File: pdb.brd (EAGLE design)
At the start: 50 x 85 mm, 38 parts, among them Q1 20MHz, Q2 IRFR5305PBF, Q3 IRFR5305PBF, U1 TSR_1-2433, U2 LTC2946CMSPBF, U3 LTC2946CMSPBF, U4 LTC2946CMSPBF, U5 ATMEGA48-20AU, U6 TXB0104, U7 AT30TS74SS8M

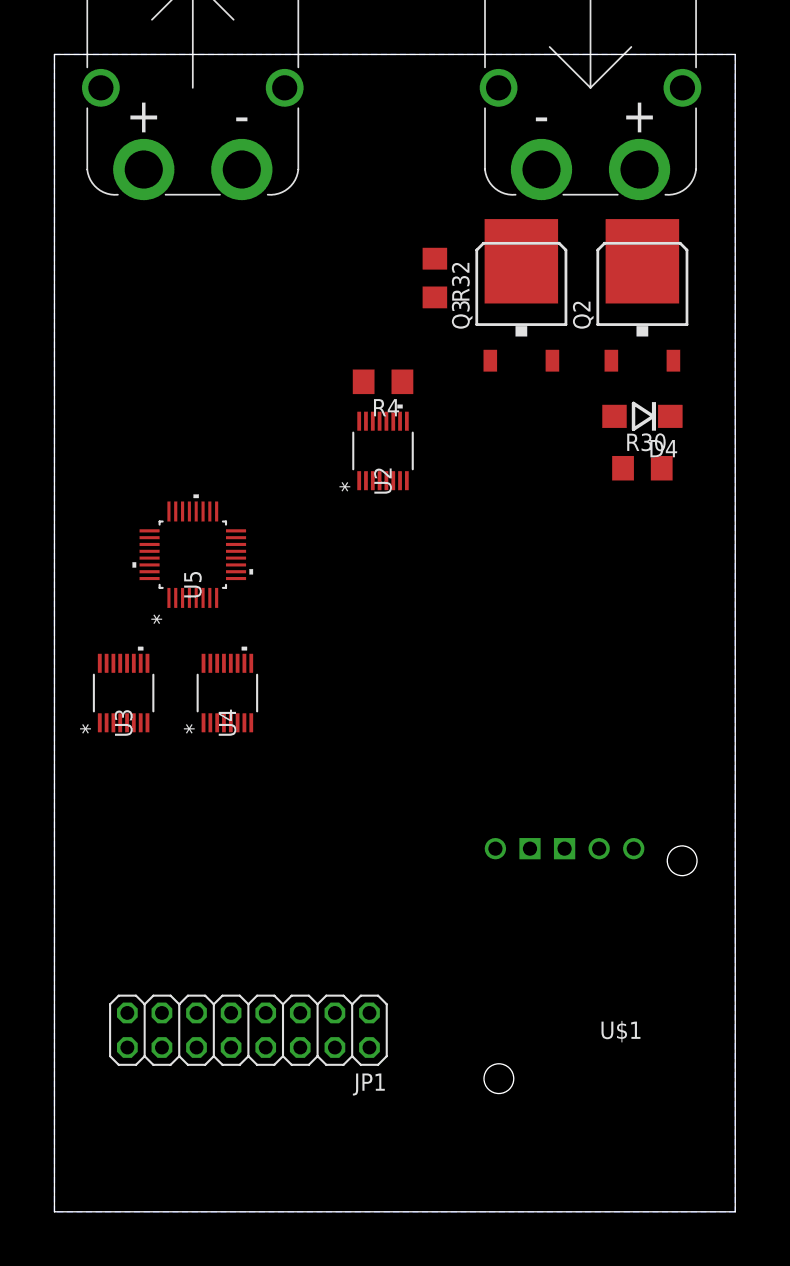
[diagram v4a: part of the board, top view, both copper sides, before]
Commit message: added mounting holes
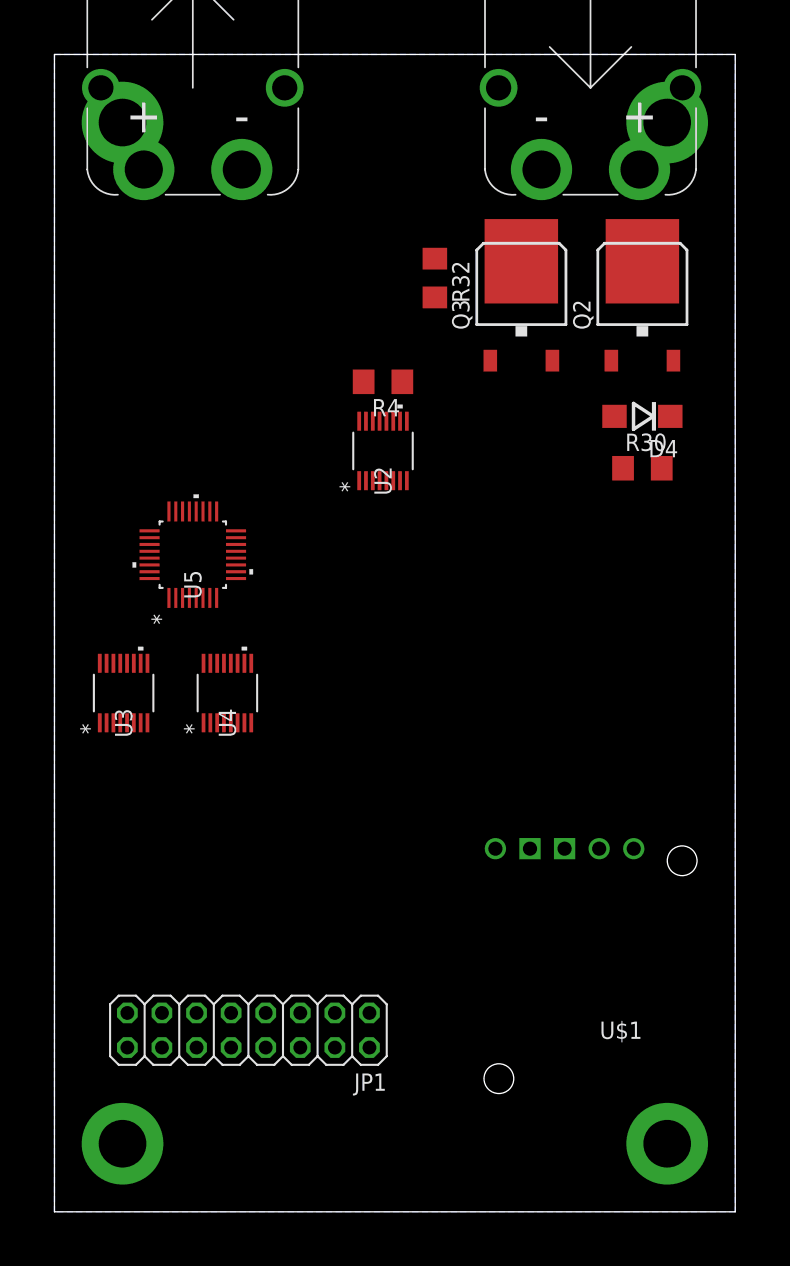
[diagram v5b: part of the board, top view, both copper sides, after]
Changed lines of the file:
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@@
 <element name="L1" library="rcl" package="0204/7" value="100µH" x="97.79" y="-7.62" rot="R90"/>
 <element name="ESC" library="amass" package="XT60PWFEMALE" value="XT60PWFEMALE" x="10.16" y="82.55"/>
-<element name="JP1" library="pinhead" library_urn="urn:adsk.eagle:library:325" package="2X08" package3d_urn="urn:adsk.eagle:package:22481/2" value="" x="14.245" y="13.335" rot="R180"/>
+<element name="JP1" library="pinhead" library_urn="urn:adsk.eagle:library:325" package="2X08" package3d_urn="urn:adsk.eagle:package:22481/2" value="" x="14.245" y="13.335" locked="yes" rot="R180"/>
 <element name="U7" library="jonas_microchip" library_urn="urn:adsk.eagle:library:891228" package="SO08" package3d_urn="urn:adsk.eagle:package:1422804/3" value="AT30TS74SS8M" x="-21.59" y="-24.13"/>
 <element name="L2" library="jonas_bourns" library_urn="urn:adsk.eagle:library:1422904" package="IND_BOURNS_RLB9012" package3d_urn="urn:adsk.eagle:package:1422907/3" value="RLB9012-221KL" x="-12.7" y="-38.1">
@@
 <vertex x="0" y="0"/>
 </polygon>
-<wire x1="37.465" y1="26.67" x2="34.925" y2="26.67" width="0" layer="19" extent="1-1"/>
-<wire x1="77.47" y1="20.32" x2="37.465" y2="26.67" width="0" layer="19" extent="1-1"/>
-<wire x1="81.96" y1="4.7022" x2="77.47" y2="20.32" width="0" layer="19" extent="1-1"/>
+<via x="5" y="80" extent="1-16" drill="3.5" diameter="6" locked="yes"/>
+<via x="45" y="80" extent="1-16" drill="3.5" diameter="6" locked="yes"/>
+<via x="5" y="5" extent="1-16" drill="3.5" diameter="6" locked="yes"/>
+<via x="45" y="5" extent="1-16" drill="3.5" diameter="6" locked="yes"/>
+<wire x1="35.77" y1="76.55" x2="27.94" y2="70.002" width="0" layer="19" extent="1-1"/>
+<wire x1="3.39" y1="-6.35" x2="5" y2="5" width="0" layer="19" extent="1-1"/>
+<wire x1="3.39" y1="-10.16" x2="3.39" y2="-6.35" width="0" layer="19" extent="1-1"/>
+<wire x1="4.33" y1="-17.78" x2="3.39" y2="-10.16" width="0" layer="19" extent="1-1"/>
+<wire x1="4.33" y1="-22.86" x2="4.33" y2="-17.78" width="0" layer="19" extent="1-1"/>
+<wire x1="4.33" y1="-27.94" x2="4.33" y2="-22.86" width="0" layer="19" extent="1-1"/>
+<wire x1="24.88056875" y1="58.0644" x2="27.94" y2="70.002" width="0" layer="19" extent="1-1"/>
+<wire x1="24.380190625" y1="58.0644" x2="24.88056875" y2="58.0644" width="0" layer="19" extent="1-1"/>
+<wire x1="23.37943125" y1="58.0644" x2="24.380190625" y2="58.0644" width="0" layer="19" extent="1-1"/>
+<wire x1="9.909809375" y1="51.435" x2="23.37943125" y2="58.0644" width="0" layer="19" extent="1-1"/>
+<wire x1="10.410190625" y1="45.085" x2="9.909809375" y2="51.435" width="0" layer="19" extent="1-1"/>
+<wire x1="9.40943125" y1="45.085" x2="10.410190625" y2="45.085" width="0" layer="19" extent="1-1"/>
+<wire x1="13.45056875" y1="40.2844" x2="10.410190625" y2="45.085" width="0" layer="19" extent="1-1"/>
+<wire x1="5.83056875" y1="40.2844" x2="9.40943125" y2="45.085" width="0" layer="19" extent="1-1"/>
+<wire x1="5.330190625" y1="40.2844" x2="5.83056875" y2="40.2844" width="0" layer="19" extent="1-1"/>
+<wire x1="22.01" y1="-17.78" x2="4.33" y2="-17.78" width="0" layer="19" extent="1-1"/>
+<wire x1="45" y1="5" x2="37.465" y2="26.67" width="0" layer="19" extent="1-1"/>
+<wire x1="63.08" y1="0" x2="45" y2="5" width="0" layer="19" extent="1-1"/>
+<wire x1="81.96" y1="4.7022" x2="63.08" y2="0" width="0" layer="19" extent="1-1"/>
+<wire x1="77.47" y1="20.32" x2="81.96" y2="4.7022" width="0" layer="19" extent="1-1"/>
 <wire x1="83.82" y1="-14.39" x2="81.96" y2="4.7022" width="0" layer="19" extent="1-1"/>
 <wire x1="87.63" y1="-14.39" x2="83.82" y2="-14.39" width="0" layer="19" extent="1-1"/>
@@
 <wire x1="73.66" y1="-25.82" x2="77.47" y2="-25.82" width="0" layer="19" extent="1-1"/>
 <wire x1="69.85" y1="-25.82" x2="73.66" y2="-25.82" width="0" layer="19" extent="1-1"/>
-<wire x1="63.08" y1="0" x2="81.96" y2="4.7022" width="0" layer="19" extent="1-1"/>
 <wire x1="107.95" y1="-17.91" x2="87.63" y2="-14.39" width="0" layer="19" extent="1-1"/>
-<wire x1="13.45056875" y1="40.2844" x2="37.465" y2="26.67" width="0" layer="19" extent="1-1"/>
-<wire x1="5.83056875" y1="40.2844" x2="13.45056875" y2="40.2844" width="0" layer="19" extent="1-1"/>
-<wire x1="5.330190625" y1="40.2844" x2="5.83056875" y2="40.2844" width="0" layer="19" extent="1-1"/>
-<wire x1="9.909809375" y1="51.435" x2="5.330190625" y2="40.2844" width="0" layer="19" extent="1-1"/>
-<wire x1="10.410190625" y1="45.085" x2="9.909809375" y2="51.435" width="0" layer="19" extent="1-1"/>
-<wire x1="9.40943125" y1="45.085" x2="10.410190625" y2="45.085" width="0" layer="19" extent="1-1"/>
-<wire x1="24.88056875" y1="58.0644" x2="5.330190625" y2="40.2844" width="0" layer="19" extent="1-1"/>
-<wire x1="24.380190625" y1="58.0644" x2="24.88056875" y2="58.0644" width="0" layer="19" extent="1-1"/>
-<wire x1="23.37943125" y1="58.0644" x2="24.380190625" y2="58.0644" width="0" layer="19" extent="1-1"/>
-<wire x1="27.94" y1="70.002" x2="24.88056875" y2="58.0644" width="0" layer="19" extent="1-1"/>
-<wire x1="35.77" y1="76.55" x2="27.94" y2="70.002" width="0" layer="19" extent="1-1"/>
-<wire x1="3.39" y1="-6.35" x2="9.40943125" y2="45.085" width="0" layer="19" extent="1-1"/>
-<wire x1="3.39" y1="-10.16" x2="3.39" y2="-6.35" width="0" layer="19" extent="1-1"/>
-<wire x1="4.33" y1="-17.78" x2="3.39" y2="-10.16" width="0" layer="19" extent="1-1"/>
-<wire x1="4.33" y1="-22.86" x2="4.33" y2="-17.78" width="0" layer="19" extent="1-1"/>
-<wire x1="4.33" y1="-27.94" x2="4.33" y2="-22.86" width="0" layer="19" extent="1-1"/>
-<wire x1="22.01" y1="-17.78" x2="4.33" y2="-17.78" width="0" layer="19" extent="1-1"/>
 </signal>
 <signal name="V+">
@@
 packages will not be understood (or retained) with this version.
 </note>
+<note version="8.5" severity="warning">
+Since Version 8.5, EAGLE supports locking for holes, vias, wires and polygons.
+The locking property on all objects of these types will not be understood in this version.
+</note>
 </compatibility>

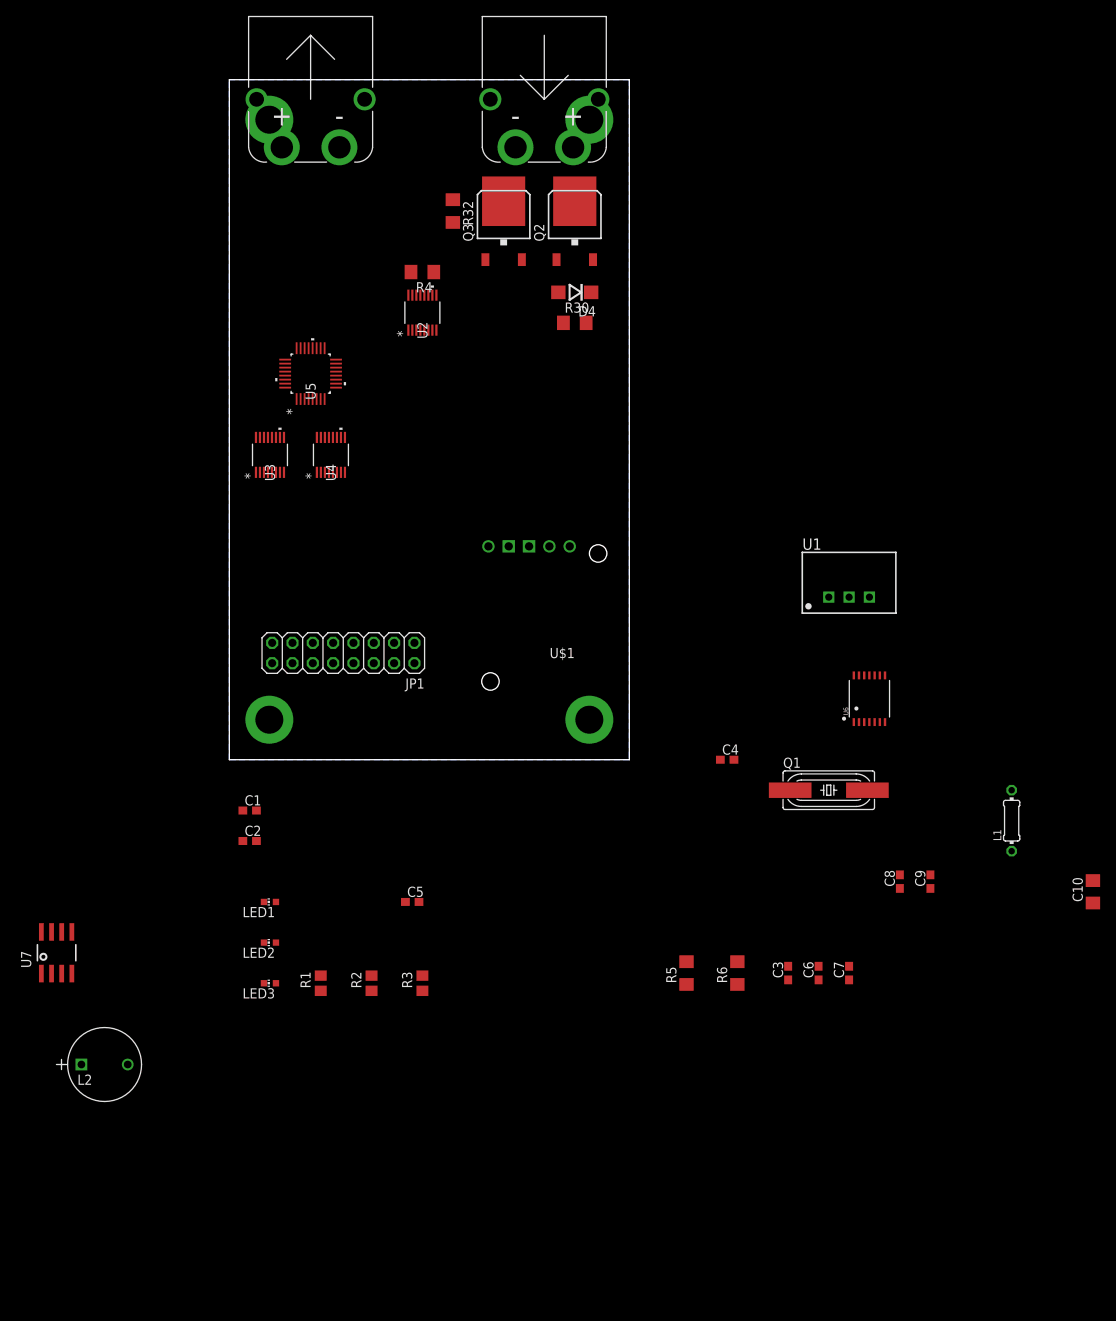
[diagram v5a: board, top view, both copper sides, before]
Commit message: AT30TS74 connected
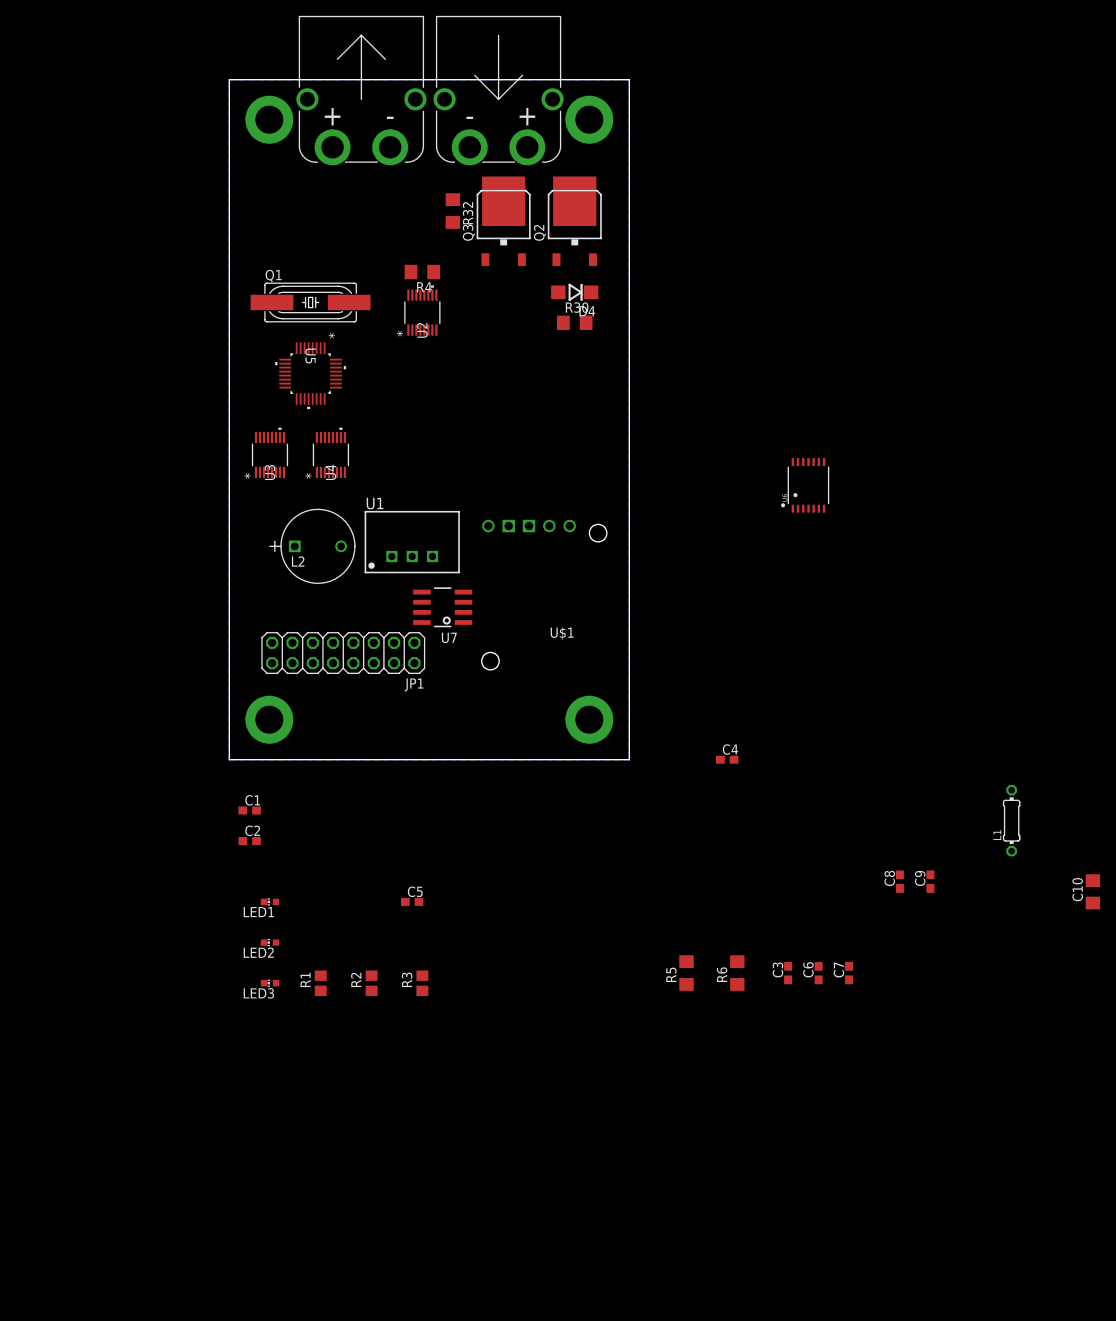
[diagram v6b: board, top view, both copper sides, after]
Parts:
- moved Q1 88.9 mm to (10.2, 57.1)
- moved L2 70.0 mm to (14.0, 26.7)
- moved U7 64.8 mm to (26.7, 19.1), turned to 90 degrees
- moved U1 54.8 mm to (22.9, 25.4)
- moved U6 27.7 mm to (72.4, 34.3)
- moved ESC 6.35 mm to (16.5, 82.5)
- moved U$2 5.71 mm to (33.7, 82.5)
- moved U$1 2.54 mm to (48.3, 30.5)
- turned U5 to 270 degrees
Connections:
- new net N$11: U7.3
- new net N$13: U7.5
- new net N$14: U7.6
- new net N$16: U7.7
- new net SCL_5V: U7.2
- new net SDA_5V: U7.1
- net +5V: now also U7.8
- net GND: now also U7.4

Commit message: Header connected, First Layout attempt
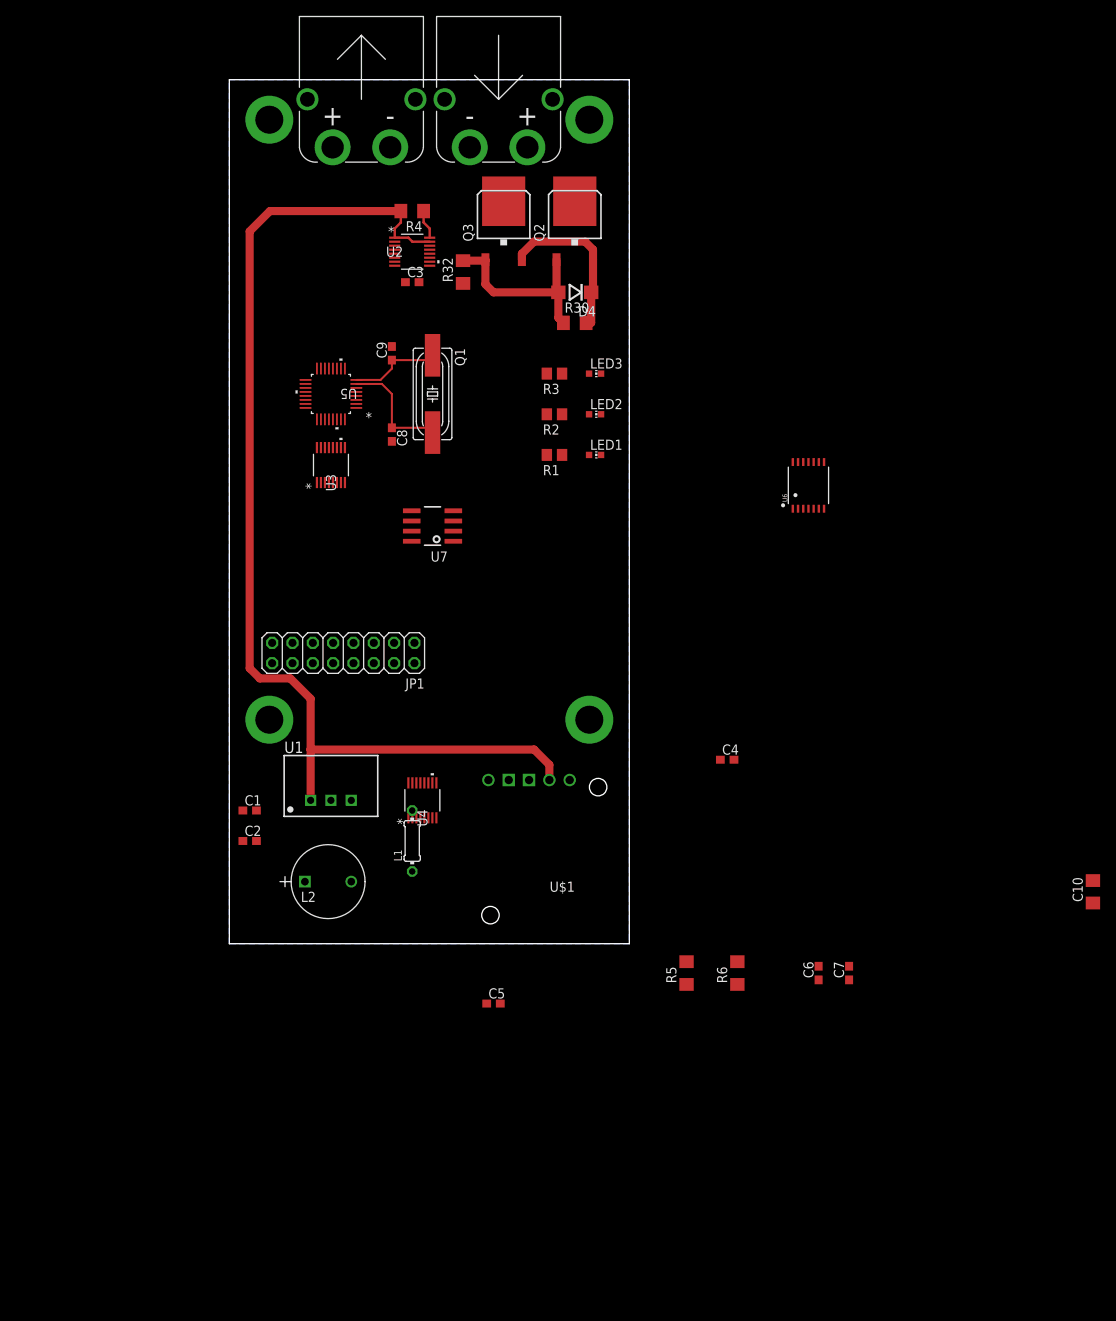
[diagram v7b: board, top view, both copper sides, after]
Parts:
- moved C3 98.3 mm to (22.9, 59.7), turned to 0 degrees
- moved C9 94.3 mm to (20.3, 50.8)
- moved LED3 86.4 mm to (45.7, 48.3), turned to 270 degrees
- moved C8 84.6 mm to (20.3, 40.6), turned to 270 degrees
- moved R3 78.0 mm to (40.6, 48.3), turned to 180 degrees
- moved LED2 77.5 mm to (45.7, 43.2), turned to 270 degrees
- moved L1 75.0 mm to (22.9, -10.2)
- moved R2 74.7 mm to (40.6, 43.2), turned to 180 degrees
- moved R1 72.2 mm to (40.6, 38.1), turned to 180 degrees
- moved LED1 69.1 mm to (45.7, 38.1), turned to 270 degrees
- moved U4 44.7 mm to (24.1, -5.08)
- moved L2 41.9 mm to (15.2, -15.2)
- moved U1 32.1 mm to (12.7, -5.08)
- moved U$1 31.8 mm to (48.3, -1.27)
- moved Q1 19.0 mm to (25.4, 45.7), turned to 270 degrees
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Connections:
- removed net MISO_3V3: U6.2
- removed net MOSI_3V3: U6.3
- removed net SS_3V3: U6.5
- new net EXT_!RST: JP1.16
- new net EXT_A0: JP1.9
- new net EXT_A3: JP1.7
- new net EXT_A4: JP1.5
- new net EXT_D1: JP1.14
- new net EXT_D2: JP1.12
- new net EXT_D9: JP1.10
- new net EXT_SCL_5V: JP1.13
- new net EXT_SDA_5V: JP1.15
- new net EXT_SPI_CLK: JP1.11, U6.4
- new net EXT_SPI_CS: JP1.8, U6.5
- new net EXT_SPI_MISO: JP1.4, U6.3
- new net EXT_SPI_MOSI: JP1.6, U6.2
- net +3V3: now also JP1.3
- net +5V: now also JP1.1
- net GND: now also JP1.2
- net SCK_5V: no longer U6.4
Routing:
- net V+: track 0.00 -> 137.2 mm
- net N$41: track 0.00 -> 23.8 mm
- net AKKU-ZWISCHEN: track 0.00 -> 20.5 mm
- net N$27: track 0.00 -> 14.5 mm
- net N$28: track 0.00 -> 11.4 mm
- net SENSE+V+: track 0.00 -> 3.64 mm
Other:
- board size 50 x 85 mm -> 50 x 108 mm
